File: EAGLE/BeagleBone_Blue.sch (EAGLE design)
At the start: 307 parts, among them J2 SERVO_HEADERS_8X, M1 JST_ZH_2, M2 JST_ZH_2, M3 JST_ZH_2, M4 JST_ZH_2, Q1 MOSFET-N, U1 TCAN1051HV, U10 TXS0108ERGYR, U13 EMMC, U2 SN74LV1T126DBVR, U3 TPD4S012DRY, U4 TPD4S012DRY, U5 24LC_32AT-I/OT, U6 SN74LVC1G07_DCK_5, U7 WL1835MODGBMOCT, U8 TPS2105_DBV_5, U9 TXS0108ERGYR, X2 SCHA5B0200, X3 USB1, X4 10118192-0001LF, Y1 24 MHz, Y2 32.768kHz

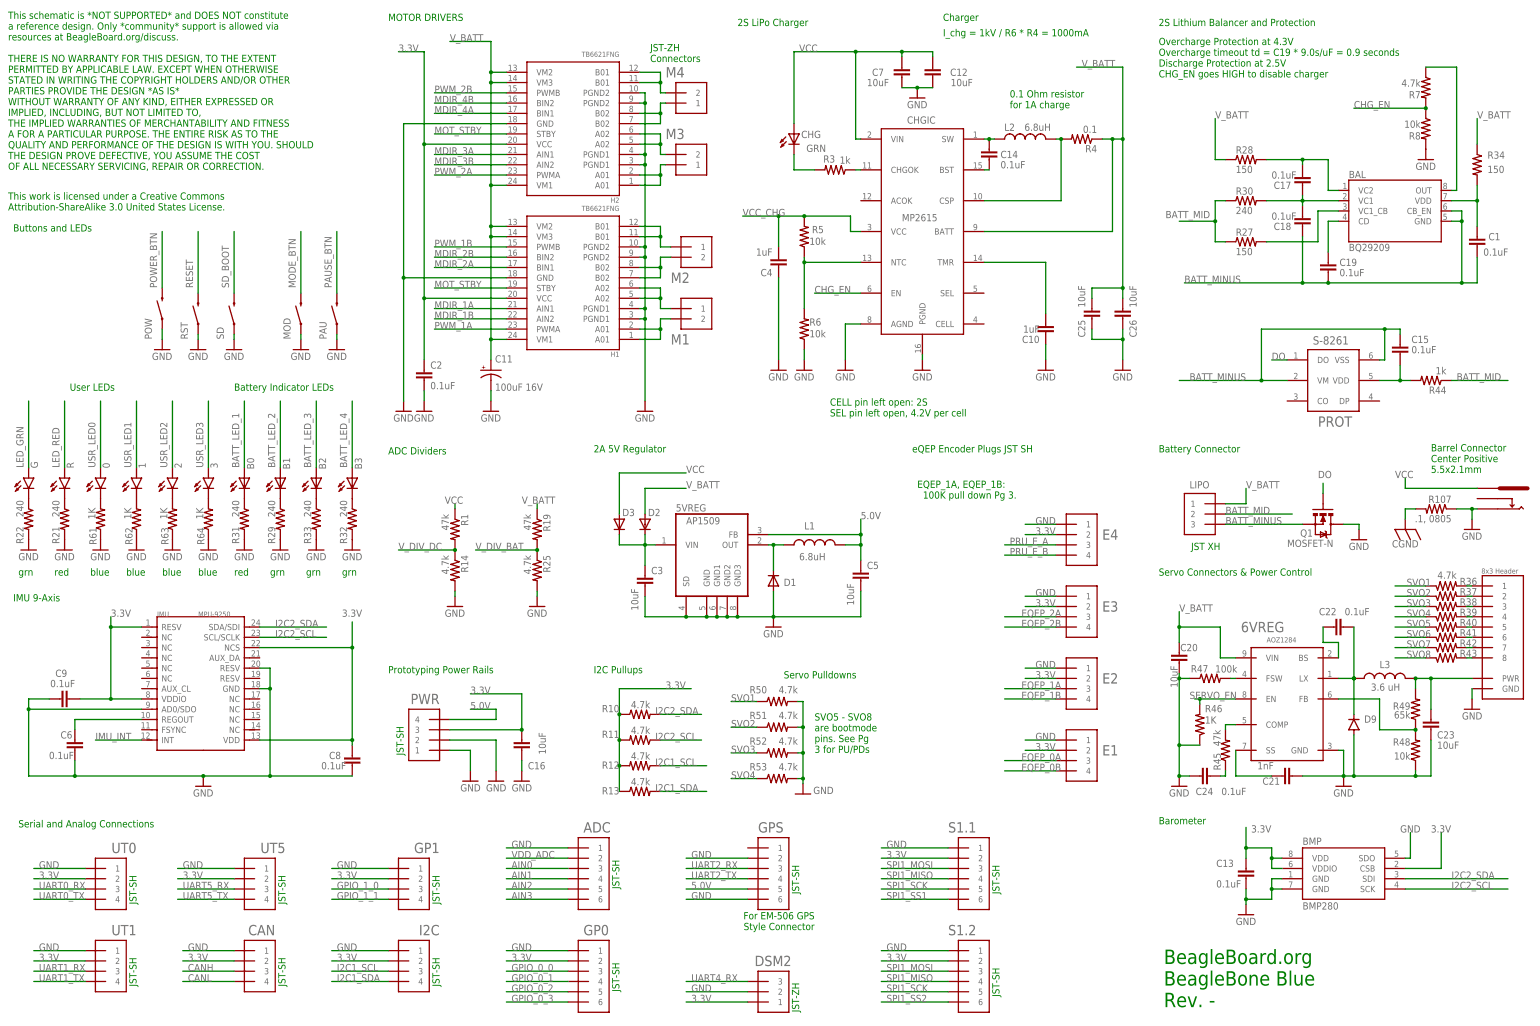
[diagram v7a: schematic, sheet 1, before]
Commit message: Updated schematics:  removed some test points; changed GPIO 1 connector to 6 pin JST; Updated EQEP layout.
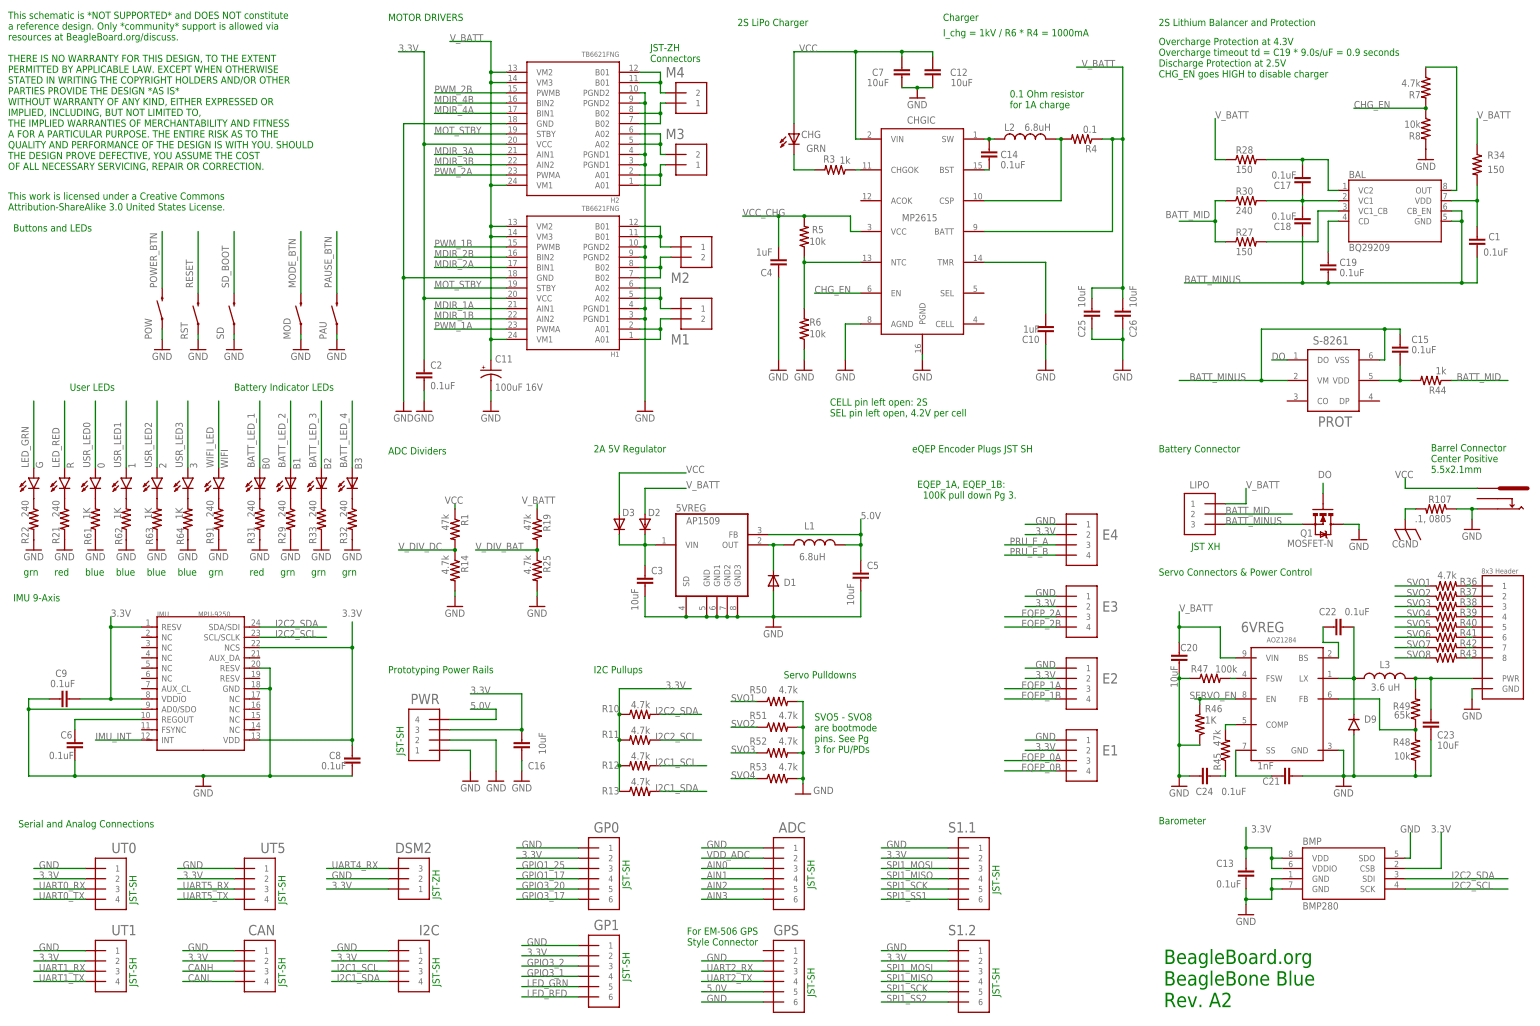
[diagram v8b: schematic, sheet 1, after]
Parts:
- removed TP11, TP2, TP3, TP4, TP6, TP7, TP8, TP9: TPB0,65, BeagleBone_Blue:TPB0,65
- GP1: value JST_SH_4 -> JST_SH_6; device Strawson_Eagle_Lib:JST_SH_4 -> Strawson_Eagle_Lib:JST_SH_6
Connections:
- net GPIO_0_0 renamed GPIO1_25
- net GPIO_0_1 renamed GPIO1_17
- net GPIO_0_2 renamed GPIO3_20
- net GPIO_0_3 renamed GPIO3_17
- net GPIO_1_0 renamed GPIO3_2
- net GPIO_1_1 renamed GPIO3_1
- removed net N$19: SIPA.L1_OUT, TP7.TP
- removed net N$21: SIPA.L2_OUT, TP9.TP
- removed net N$23: SIPA.L3_OUT, TP11.TP
- removed net N$72: SIPE.VDD_3V3A12, TP2.TP
- removed net N$73: SIPE.VDD_MPU6, TP3.TP
- removed net N$76: SIPE.VDD_PLL2, TP4.TP
- removed net N$78: SIPE.VDD_CORE20, TP6.TP
- removed net N$80: SIPE.VDDS_DDR1, TP8.TP
- net LED_GRN: now also GP1.5
- net LED_RED: now also GP1.6
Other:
- note added: "BeagleBoard.org BeagleBone Blue Rev. A2"
- note removed: "BeagleBoard.org BeagleBone Blue Rev. -"
- moved on the sheet: 0, 1, 2, 3, ADC, B0, B1, B2, DSM2, G, GP0, GPS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
